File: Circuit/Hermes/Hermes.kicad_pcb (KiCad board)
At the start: 2 copper layers, 73.8 x 38.1 mm, 3 parts, among them U1 VL53L0CXV0DH1, U2 XIAO-RP2040-DIP

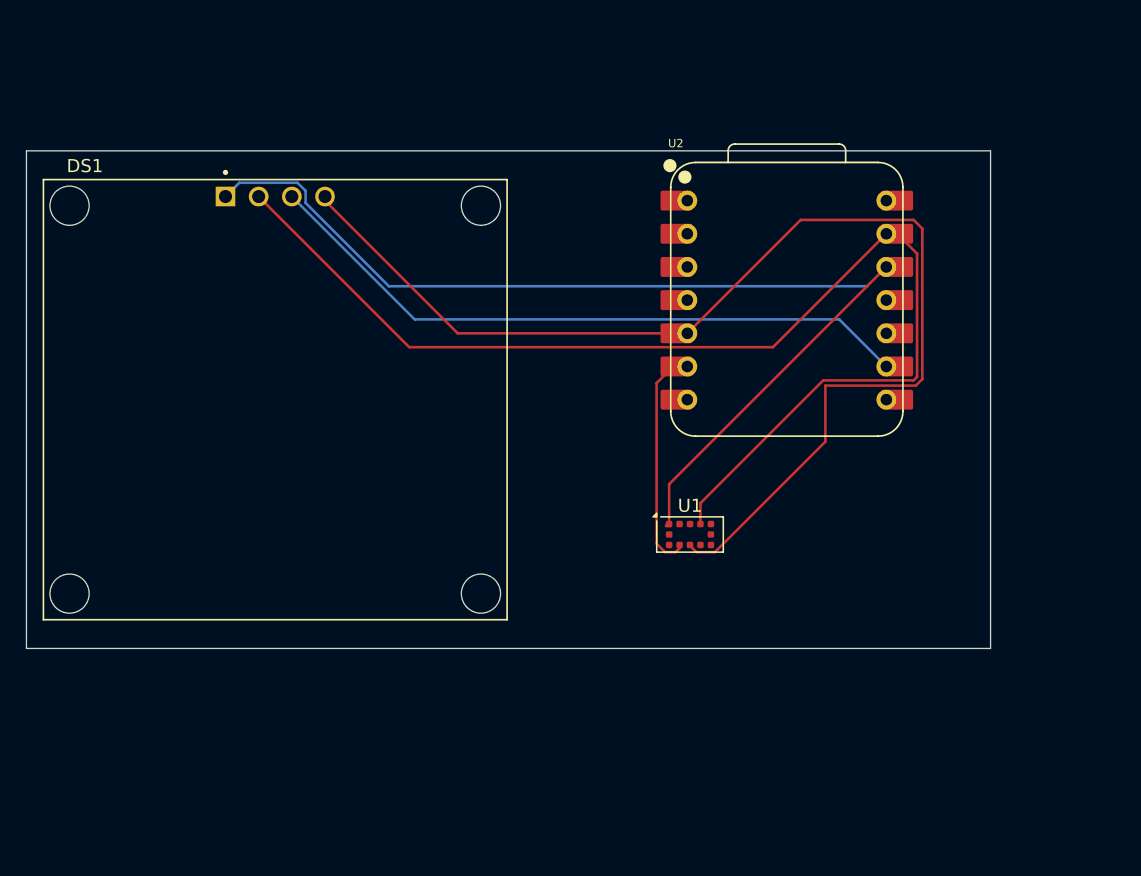
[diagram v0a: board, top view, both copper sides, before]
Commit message: Add new components and update code for temperature and distance measurement
- Updated fp-lib-table and sym-lib-table to include new libraries: LM393, DHT11, BUTT-2, HC-SR04, and ARDUINO_NANO.
- Added LM393 component files including symbol and footprint.
- Created a redirection HTML file for LM393 import instructions.
- Modified the Arduino code to integrate DHT11 sensor for temperature and humidity readings.
- Implemented button functionality to toggle between temperature and distance display modes.
- Updated display logic to show sensor data based on the selected mode.
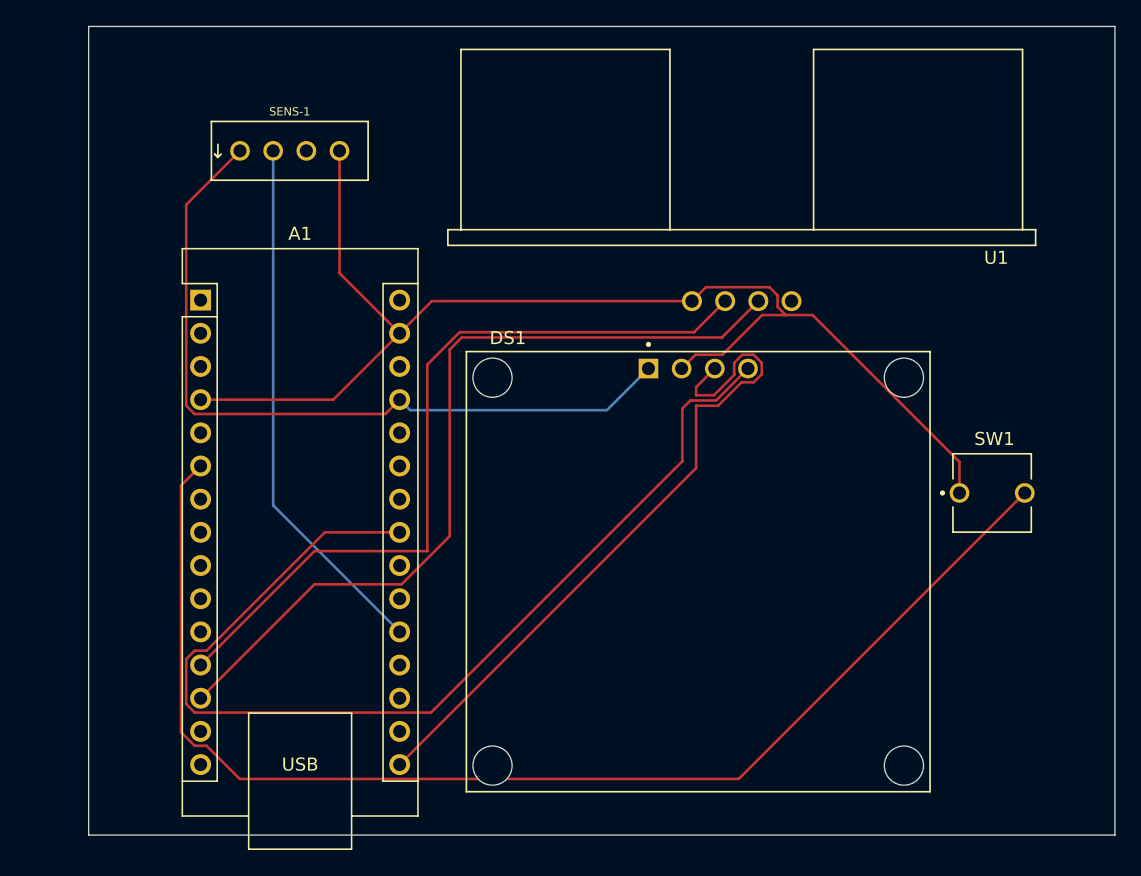
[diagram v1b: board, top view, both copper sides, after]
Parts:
- removed U2: XIAO-RP2040-DIP, OPL_Kicad:XIAO-RP2040-DIP
- added A1: Arduino_Nano_Every, Module:Arduino_Nano, F.Cu at (146.7, 87.6)
- added SENS-1: DHT11, DHT11:SENSOR-DHT11, F.Cu at (153.5, 76.2)
- added SW1: SW_Push, BUTT-2:SW_BUTT-2, F.Cu at (207.3, 102.4)
- U1: value VL53L0CXV0DH1 -> HC-SR04; footprint Sensor_Distance:ST_VL53L1x -> HC-SR04:XCVR_HC-SR04
- moved DS1 35.0 mm to (184.8, 108.4)
- moved U1 18.3 mm to (188.1, 87.7), turned to 180 degrees
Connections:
- DS1 pad 4: Net-(DS1-SDA) -> Net-(A1-SDA/A4)
- U1 pad 2: unconnected-(U1-AVSSVCSEL-Pad2) -> Net-(A1-D10)
- U1 pad 3: Net-(DS1-GND) -> Net-(A1-D9)
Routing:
- net Net-(A1-D3): track 0.00 -> 96.2 mm
- net Net-(DS1-SDA): track 90.9 -> 0.00 mm
- net Net-(A1-SDA/A4): track 0.00 -> 80.4 mm
- net Net-(A1-D10): track 0.00 -> 63.7 mm
- net Net-(A1-D9): track 0.00 -> 60.1 mm
- net Net-(A1-A1): track 0.00 -> 40.8 mm
- net Net-(A1-+5V): track 82.0 -> 59.0 mm
- net Net-(U1-SCL): track 17.6 -> 0.00 mm
- net Net-(DS1-GND): track 90.2 -> 95.7 mm
- net Net-(A1-SCK): track 50.9 -> 53.6 mm
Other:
- board size 73.8 x 38.1 mm -> 78.6 x 61.9 mm
